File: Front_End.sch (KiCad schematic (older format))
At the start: 15 parts

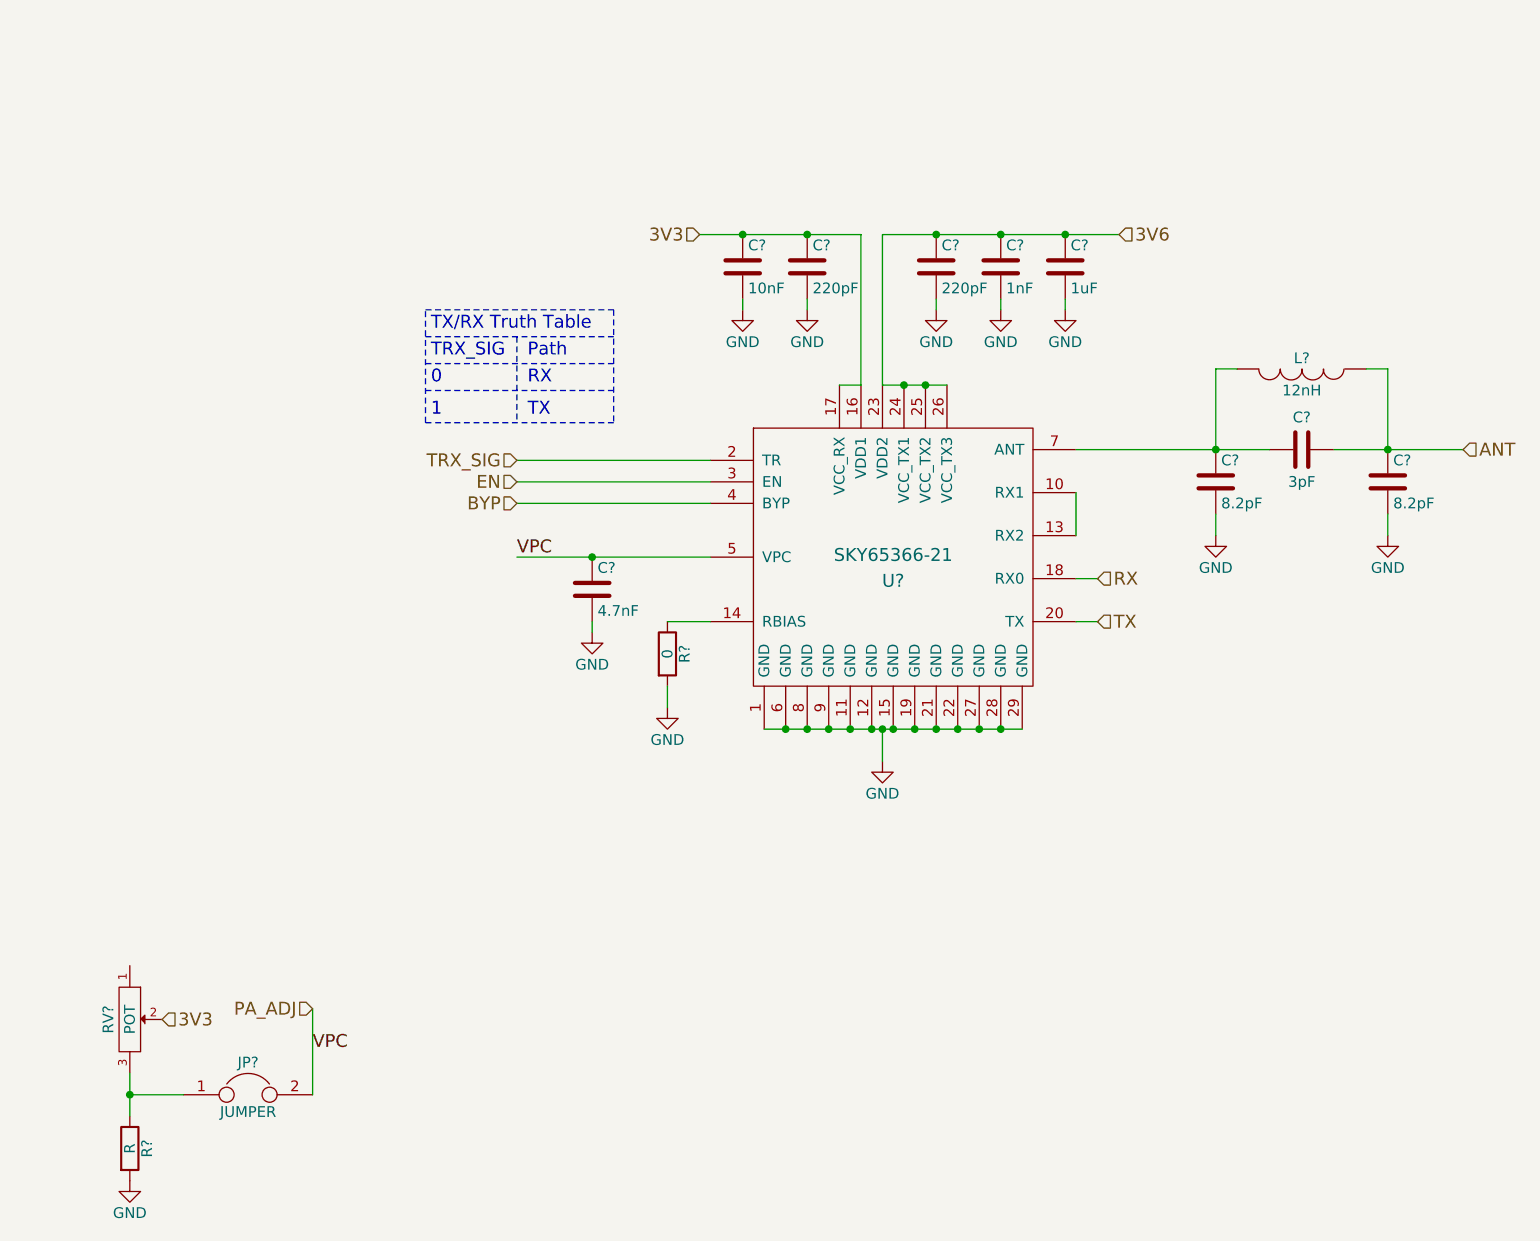
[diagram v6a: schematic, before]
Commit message: added switches for various option and nmos array to control status leds
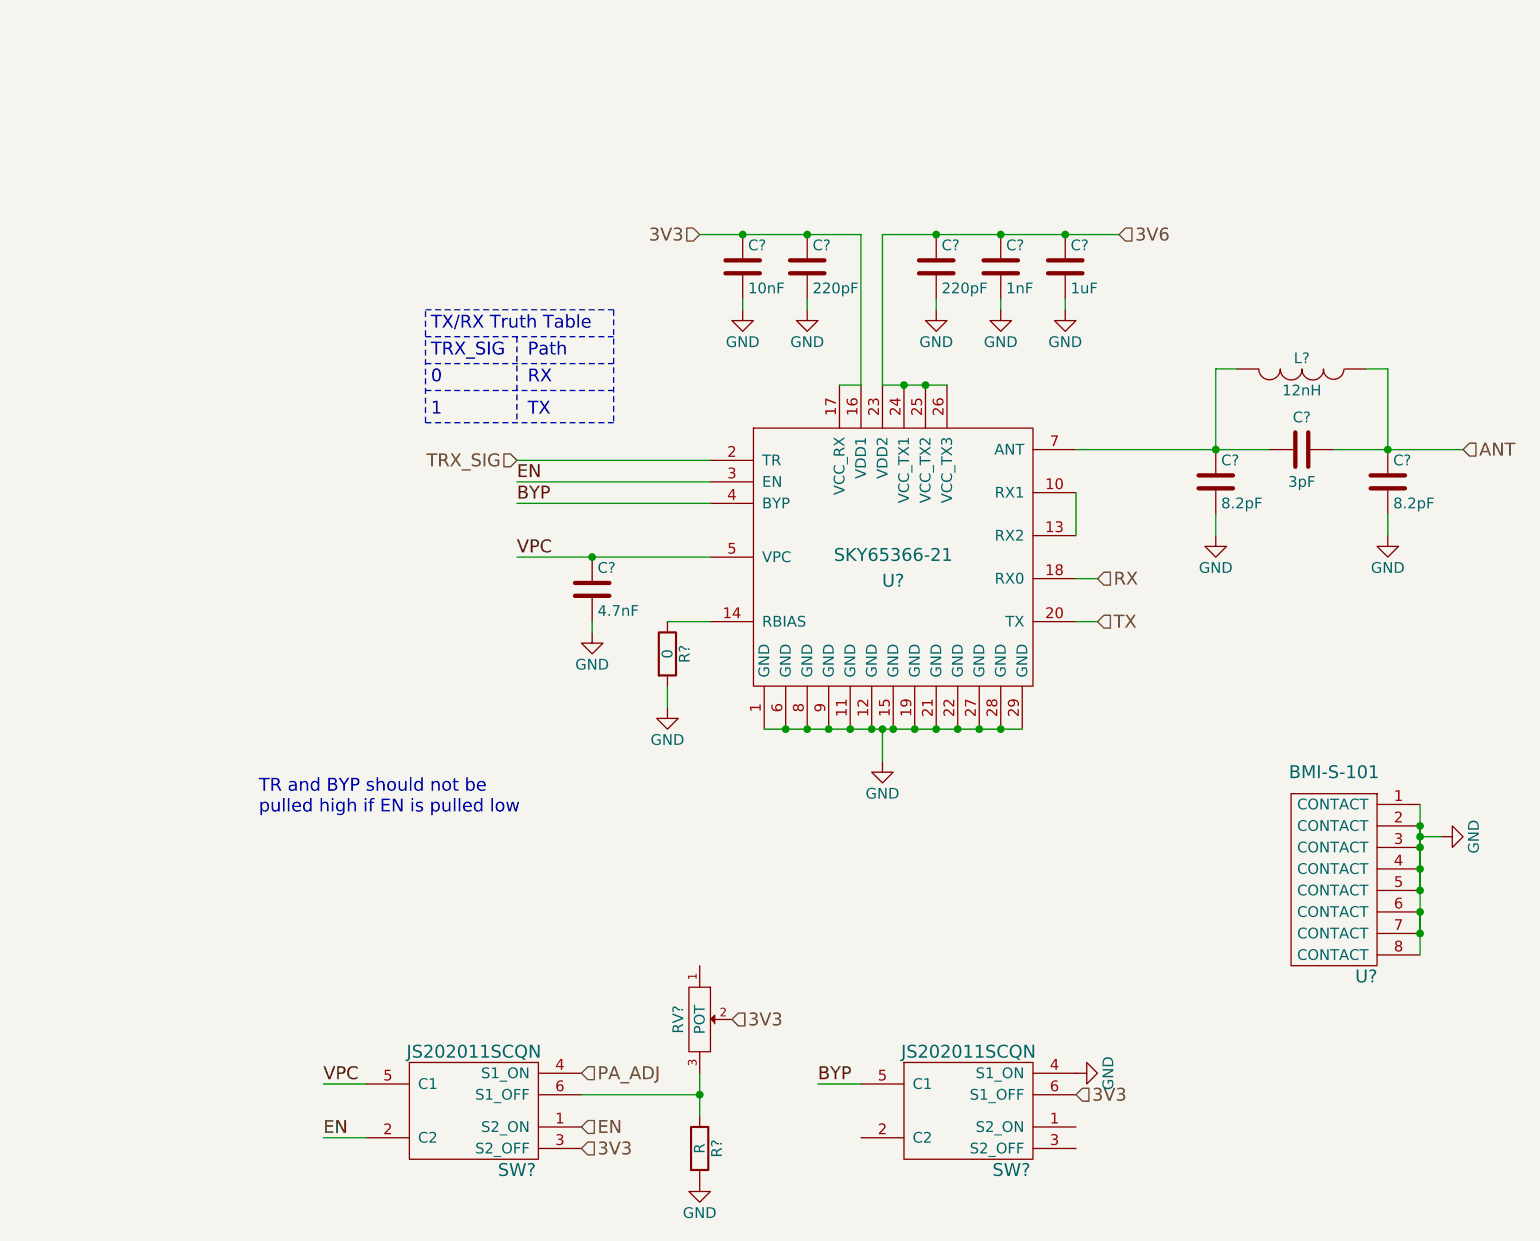
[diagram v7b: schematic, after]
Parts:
- removed JP?: JUMPER, symbol JUMPER
- added SW? (x2): JS202011SCQN, symbol JS202011SCQN
- added U?: BMI-S-101, symbol BMI-S-101
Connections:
- net 3V3: now also SW?.3 (S2_OFF), SW?.6 (S1_OFF)
- net BYP: now also SW?.5 (C1)
- net EN: now also SW?.1 (S2_ON), SW?.2 (C2)
- net GND: now also SW?.4 (S1_ON), U?.1 (CONTACT), U?.2 (CONTACT), U?.3 (CONTACT), U?.4 (CONTACT), U?.5 (CONTACT), U?.6 (CONTACT), U?.7 (CONTACT), U?.8 (CONTACT)
- net PA_ADJ: now also SW?.4 (S1_ON); no longer C?.1, U?.5 (VPC)
- net at R?.1, RV?.3: now also SW?.6 (S1_OFF)
- new net VPC: C?.1, SW?.5 (C1), U?.5 (VPC)
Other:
- note added: "TR and BYP should not be \npulled high if EN is pulled low"
- moved on the sheet: R?, RV?
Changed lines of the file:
@@
 Text HLabel 8200 3200 2    60   Input ~ 0
 ANT
-Text HLabel 2850 5800 0    60   Input ~ 0
+Text HLabel 4100 6100 2    60   Input ~ 0
 PA_ADJ
 Text HLabel 6500 4000 2    60   Input ~ 0
@@
 	5500 2900 5500 2200
 Connection ~ 5750 2200
-Text HLabel 3800 3450 0    60   Input ~ 0
-BYP
 Text HLabel 3800 3250 0    60   Input ~ 0
 TRX_SIG
@@
 Wire Wire Line
 	4700 3350 3800 3350
-Text HLabel 3800 3350 0    60   Input ~ 0
+Text HLabel 4100 6350 2    60   Input ~ 0
 EN
 Text Notes 3400 2775 0    60   ~ 0
@@
 	7750 2825 7850 2825
 $Comp
-L JUMPER JP?
-U 1 1 587C256C
-P 2550 6200
-F 0 "JP?" H 2550 6350 50  0000 C CNN
-F 1 "JUMPER" H 2550 6120 50  0000 C CNN
-F 2 "" H 2550 6200 50  0000 C CNN
-F 3 "" H 2550 6200 50  0000 C CNN
-	1    2550 6200
-	1    0    0    -1
-$EndComp
-$Comp
 L R R?
 U 1 1 587C3C10
-P 2000 6450
-F 0 "R?" V 2080 6450 50  0000 C CNN
-F 1 "R" V 2000 6450 50  0000 C CNN
-F 2 "" V 1930 6450 50  0000 C CNN
-F 3 "" H 2000 6450 50  0000 C CNN
-	1    2000 6450
+P 4650 6450
+F 0 "R?" V 4730 6450 50  0000 C CNN
+F 1 "R" V 4650 6450 50  0000 C CNN
+F 2 "" V 4580 6450 50  0000 C CNN
+F 3 "" H 4650 6450 50  0000 C CNN
+	1    4650 6450
 	1    0    0    -1
 $EndComp
@@
 L GND #PWR?
 U 1 1 587C3C45
-P 2000 6600
-F 0 "#PWR?" H 2000 6350 50  0001 C CNN
-F 1 "GND" H 2000 6450 50  0000 C CNN
-F 2 "" H 2000 6600 50  0000 C CNN
-F 3 "" H 2000 6600 50  0000 C CNN
-	1    2000 6600
-	1    0    0    -1
-$EndComp
-Wire Wire Line
-	2000 6100 2000 6300
-Wire Wire Line
-	2250 6200 2000 6200
-Connection ~ 2000 6200
-Wire Wire Line
-	2850 6200 2850 5800
+P 4650 6600
+F 0 "#PWR?" H 4650 6350 50  0001 C CNN
+F 1 "GND" H 4650 6450 50  0000 C CNN
+F 2 "" H 4650 6600 50  0000 C CNN
+F 3 "" H 4650 6600 50  0000 C CNN
+	1    4650 6600
+	1    0    0    -1
+$EndComp
+Wire Wire Line
+	4650 6100 4650 6300
+Connection ~ 4650 6200
 Text Label 3800 3700 0    60   ~ 0
 VPC
-Text Label 2850 6000 0    60   ~ 0
+Text Label 2900 6150 0    60   ~ 0
 VPC
-Text HLabel 2150 5850 2    60   Input ~ 0
+Text HLabel 4800 5850 2    60   Input ~ 0
 3V3
 $Comp
 L POT RV?
 U 1 1 587CA745
-P 2000 5850
-F 0 "RV?" H 2000 5750 50  0000 C CNN
-F 1 "POT" H 2000 5850 50  0000 C CNN
-F 2 "" H 2000 5850 50  0000 C CNN
-F 3 "" H 2000 5850 50  0000 C CNN
-	1    2000 5850
+P 4650 5850
+F 0 "RV?" H 4650 5750 50  0000 C CNN
+F 1 "POT" H 4650 5850 50  0000 C CNN
+F 2 "" H 4650 5850 50  0000 C CNN
+F 3 "" H 4650 5850 50  0000 C CNN
+	1    4650 5850
 	0    1    1    0
 $EndComp
+$Comp
+L JS202011SCQN SW?
+U 1 1 587E3043
+P 3600 6150
+F 0 "SW?" H 3800 5750 60  0000 C CNN
+F 1 "JS202011SCQN" H 3600 6300 60  0000 C CNN
+F 2 "" H 3600 6150 60  0000 C CNN
+F 3 "" H 3600 6150 60  0000 C CNN
+	1    3600 6150
+	1    0    0    -1
+$EndComp
+Wire Wire Line
+	3100 6150 2900 6150
+Wire Wire Line
+	4650 6200 4100 6200
+Text HLabel 4100 6450 2    60   Input ~ 0
+3V3
+Text Label 3800 3350 0    60   ~ 0
+EN
+Wire Wire Line
+	3100 6400 2900 6400
+Text Label 2900 6400 0    60   ~ 0
+EN
+Text Notes 2600 4900 0    60   ~ 0
+TR and BYP should not be \npulled high if EN is pulled low
+$Comp
+L JS202011SCQN SW?
+U 1 1 58828A5A
+P 5900 6150
+F 0 "SW?" H 6100 5750 60  0000 C CNN
+F 1 "JS202011SCQN" H 5900 6300 60  0000 C CNN
+F 2 "" H 5900 6150 60  0000 C CNN
+F 3 "" H 5900 6150 60  0000 C CNN
+	1    5900 6150
+	1    0    0    -1
+$EndComp
+Wire Wire Line
+	5400 6150 5200 6150
+Text Label 5200 6150 0    60   ~ 0
+BYP
+Text Label 3800 3450 0    60   ~ 0
+BYP
+Text HLabel 6400 6200 2    60   Input ~ 0
+3V3
+$Comp
+L GND #PWR?
+U 1 1 58829BDE
+P 6400 6100
+F 0 "#PWR?" H 6400 5850 50  0001 C CNN
+F 1 "GND" H 6400 5950 50  0000 C CNN
+F 2 "" H 6400 6100 50  0000 C CNN
+F 3 "" H 6400 6100 50  0000 C CNN
+	1    6400 6100
+	0    -1   -1   0
+$EndComp
+$Comp
+L BMI-S-101 U?
+U 1 1 5882B6C7
+P 7600 4850
+F 0 "U?" H 7750 4050 60  0000 C CNN
+F 1 "BMI-S-101" H 7600 5000 60  0000 C CNN
+F 2 "" H 7600 4850 60  0000 C CNN
+F 3 "" H 7600 4850 60  0000 C CNN
+	1    7600 4850
+	1    0    0    -1
+$EndComp
+$Comp
+L GND #PWR?
+U 1 1 5882B8A8
+P 8100 5000
+F 0 "#PWR?" H 8100 4750 50  0001 C CNN
+F 1 "GND" H 8100 4850 50  0000 C CNN
+F 2 "" H 8100 5000 50  0000 C CNN
+F 3 "" H 8100 5000 50  0000 C CNN
+	1    8100 5000
+	0    -1   -1   0
+$EndComp
+Wire Wire Line
+	8000 4850 8000 5550
+Wire Wire Line
+	8000 4950 8000 5250
+Connection ~ 8000 5050
+Connection ~ 8000 4950
+Connection ~ 8000 5150
+Connection ~ 8000 5250
+Wire Wire Line
+	8000 5350 8000 5450
+Connection ~ 8000 5450
+Connection ~ 8000 5350
+Wire Wire Line
+	8100 5000 8000 5000
+Connection ~ 8000 5000
 $EndSCHEMATC
